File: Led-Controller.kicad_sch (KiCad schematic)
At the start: 62 parts, among them J1 Barrel_Jack, J2 Screw_Terminal, J3 Program, Q1 CSD18540Q5B, Q2 CSD18540Q5B, Q3 CSD18540Q5B, Q4 CSD18540Q5B, Q5 CSD18540Q5B, Q6 CSD18540Q5B, U1 1ED44175N01BXTSA1, U2 1ED44175N01BXTSA1, U3 TPS5430DDA, U4 1ED44175N01BXTSA1, U5 1ED44175N01BXTSA1, U6 TPS5430DDA, U7 1ED44175N01BXTSA1, U8 ESP32-WROOM-32E

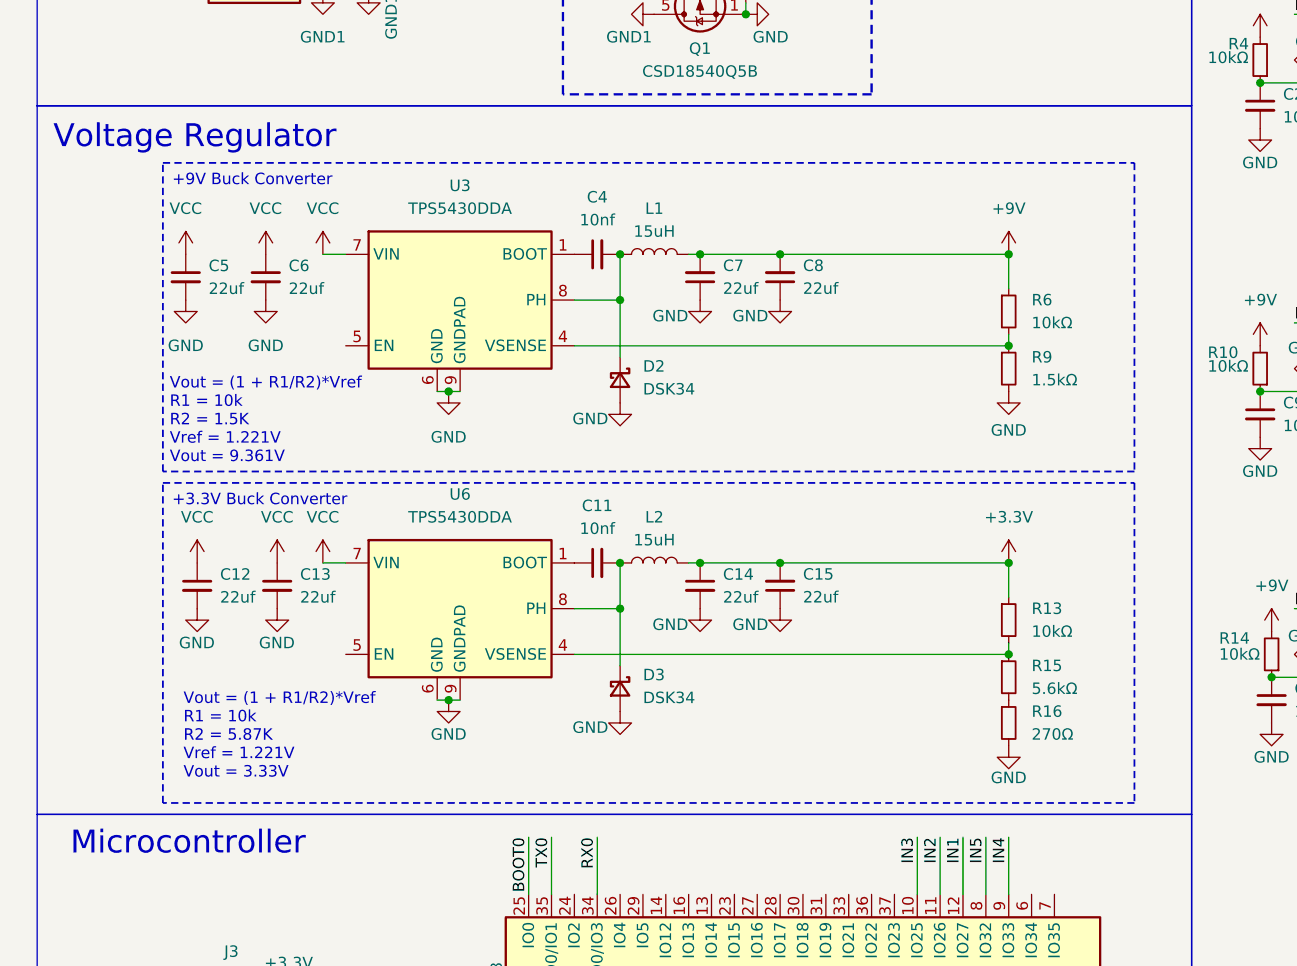
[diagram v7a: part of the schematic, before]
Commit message: Added: Ferrite bead for conduction EMI filtering
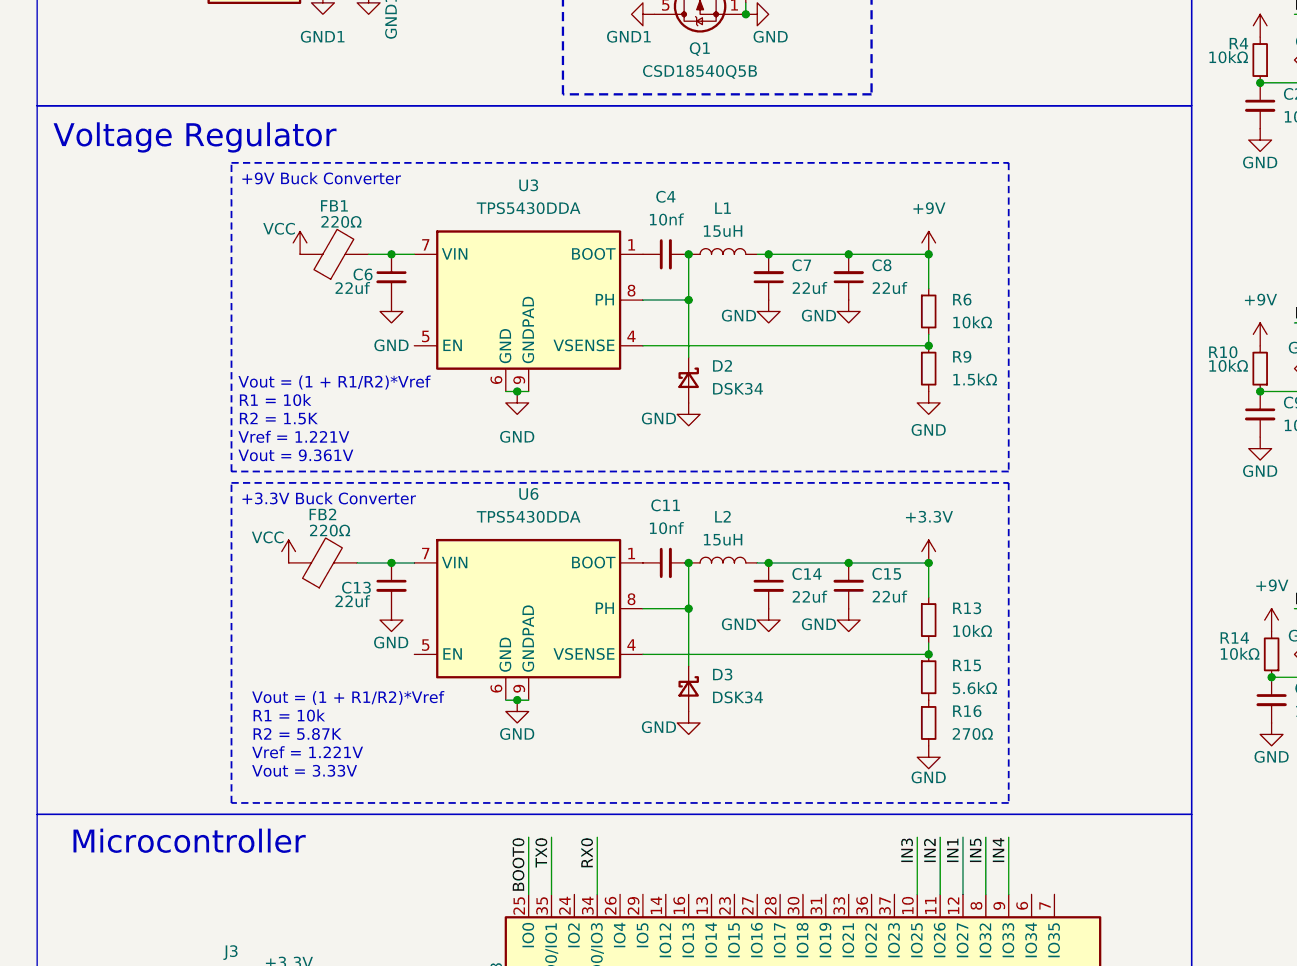
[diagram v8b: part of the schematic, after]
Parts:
- removed C12, C5: 22uf, Capacitor_SMD:C_0805_2012Metric_Pad1.18x1.45mm_HandSolder, symbol Device:C_Small
- added FB1, FB2: 220Ω, Resistor_SMD:R_0805_2012Metric, symbol Device:FerriteBead
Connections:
- net VCC: now also FB1.1, FB2.1; no longer C13.1, C6.1, U3.7 (VIN), U6.7 (VIN)
- new net: C13.1, FB2.2, U6.7 (VIN)
- new net: C6.1, FB1.2, U3.7 (VIN)
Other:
- moved on the sheet: C11, C13, C14, C15, C4, C6, C7, C8, D2, D3, L1, L2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
